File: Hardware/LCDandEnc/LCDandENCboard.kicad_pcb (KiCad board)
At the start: 2 copper layers, 18 parts, among them J1 LCD4x20, J2 LCD4x20, U1 74HC14

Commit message: layout and BOM
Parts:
- removed 1U2: 0,1U, Capacitors_SMD:C_0805_HandSoldering
- added C4: 1u, Capacitors_SMD:C_0805_HandSoldering, F.Cu at (160.9, 108.9)
- added C5: 100n, Capacitors_SMD:C_0805_HandSoldering, F.Cu at (161.0, 103.7)
- added REF**: JUMPER 5MM, Libs:JUMPER_5MM, F.Cu at (153.1, 112.4)
- added U2: XC6206P332MR, TO_SOT_Packages_SMD:TSOT-23_HandSoldering, F.Cu at (156.7, 106.2)
- J1: value LCD4x20 -> Connection to mainBoard; footprint Pin_Headers:Pin_Header_Straight_1x04_Pitch2.54mm -> Pin_Headers:Pin_Header_Straight_1x07_Pitch2.54mm
- moved 1U1 62.2 mm to (134.0, 107.1), turned to 90 degrees
- moved J1 61.2 mm to (133.0, 114.6), turned to 90 degrees
- moved J2 42.0 mm to (152.3, 114.6), turned to 90 degrees
- moved D1 24.0 mm to (155.8, 95.8)
- moved R2 22.0 mm to (152.5, 90.5), turned to 270 degrees
- moved C1 21.6 mm to (159.0, 95.5)
- moved ROT1 20.1 mm to (141.2, 77.7)
- moved R1 19.0 mm to (152.4, 95.8)
- moved U1 15.2 mm to (139.5, 105.0), turned to 180 degrees
- moved C3 13.9 mm to (150.0, 95.7), turned to 90 degrees
- moved R4 12.2 mm to (147.4, 87.5)
- moved R5 11.7 mm to (135.7, 94.8), turned to 270 degrees
- moved C2 9.68 mm to (130.0, 95.0), turned to 90 degrees
- moved D3 9.44 mm to (147.3, 95.6), turned to 90 degrees
- moved D2 7.96 mm to (132.9, 94.6), turned to 90 degrees
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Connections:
- 1U1 pad 1: VCC -> +3V3
- J1 pad 1: Rot_Enc_SW -> GND
- J1 pad 2: Rot_Enc_A -> Rot_Enc_B
- J1 pad 3: Rot_Enc_B -> Rot_Enc_A
- J1 pad 4: (no net) -> Rot_Enc_SW
- J2 pad 1: VCC -> +5V
- J2 pad 2: (no net) -> SCL
- J2 pad 3: (no net) -> SDA
- R2 pad 1: VCC -> +3V3
- R3 pad 1: VCC -> +3V3
- R4 pad 1: VCC -> +3V3
- U1 pad 14: VCC -> (no net)
- U1 pad 3: Net-(C2-Pad1) -> (no net)
- U1 pad 4: Rot_Enc_B -> (no net)
- U1 pad 8: (no net) -> Rot_Enc_B
- U1 pad 9: (no net) -> Net-(C2-Pad1)
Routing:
- net +3V3: track 0.00 -> 125.3 mm
- net GND: track 93.0 -> 123.9 mm
- net Net-(C2-Pad1): track 42.0 -> 14.0 mm
- net Net-(C1-Pad1): track 18.6 -> 39.5 mm
- net SCL: track 0.00 -> 18.8 mm
- net +5V: track 0.00 -> 16.5 mm
- net Rot_Enc_B: track 0.00 -> 16.1 mm
- net SDA: track 0.00 -> 15.0 mm
- net Rot_Enc_A: track 0.00 -> 14.6 mm
- net Net-(D1-Pad1): track 8.68 -> 20.4 mm
- net Net-(D2-Pad2): track 24.2 -> 14.9 mm
- net Rot_Enc_SW: track 0.00 -> 8.67 mm
- net VCC: track 8.47 -> 0.00 mm
- net Net-(D3-Pad2): track 20.5 -> 15.4 mm
- net Net-(C3-Pad1): track 14.0 -> 15.5 mm
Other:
- board outline added: 38 x 52.8 mm
- board text added: "LCD/ROTENC 25/3-18"

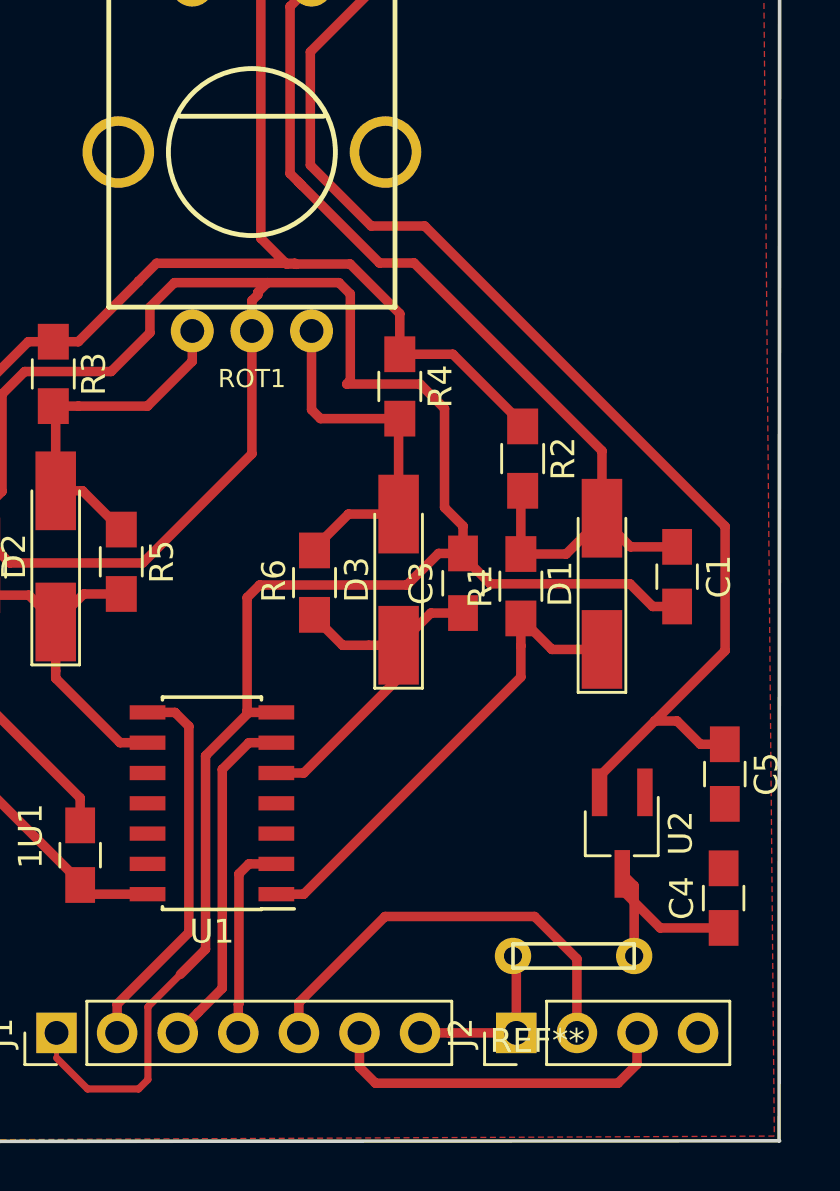
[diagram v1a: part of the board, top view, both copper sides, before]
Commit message: Bad I2C pinout
Swappe some pins around to match the i2c lcd board
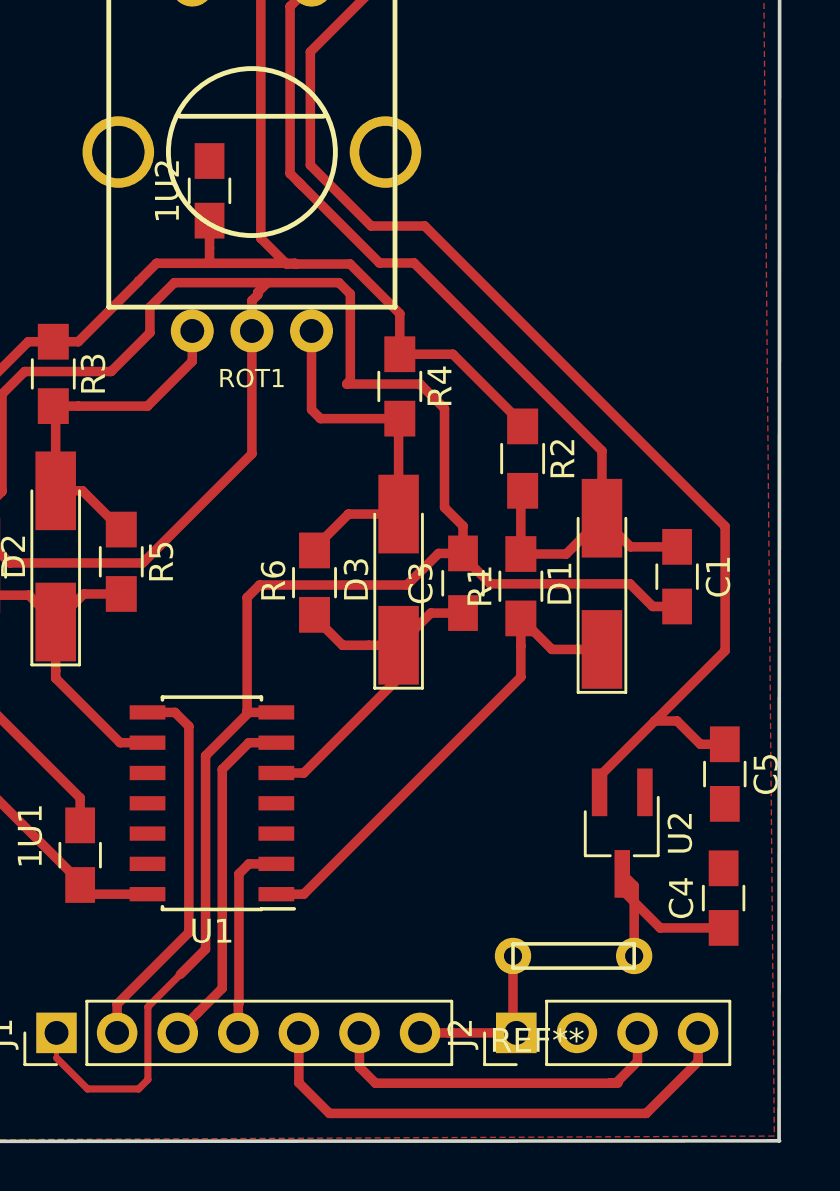
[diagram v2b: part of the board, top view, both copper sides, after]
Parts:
- added 1U2: 0,1U, Capacitors_SMD:C_0805_HandSoldering, F.Cu at (139.4, 79.3)
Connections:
- J2 pad 2: SCL -> GND
- J2 pad 4: GND -> SCL
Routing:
- net SCL: track 18.8 -> 21.5 mm
- net +3V3: track 125.3 -> 127.1 mm
- net GND: track 123.9 -> 124.4 mm
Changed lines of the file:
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@@
 (kicad_pcb (version 4) (host pcbnew 4.0.7)
   (general
-    (links 0)
-    (no_connects 8)
-    (area 125.25 66.299999 163.925 124.494048)
+    (links 46)
+    (no_connects 6)
+    (area 125.274999 66.299999 163.375001 119.200001)
     (thickness 1.6)
     (drawings 5)
-    (tracks 181)
+    (tracks 187)
     (zones 0)
-    (modules 21)
+    (modules 22)
     (nets 15)
   )
@@
       (net 13 +5V))
     (pad 2 thru_hole oval (at 0 2.54 90) (size 1.7 1.7) (drill 1) (layers *.Cu *.Mask)
-      (net 12 SCL))
+      (net 1 GND))
     (pad 3 thru_hole oval (at 0 5.08 90) (size 1.7 1.7) (drill 1) (layers *.Cu *.Mask)
       (net 14 SDA))
     (pad 4 thru_hole oval (at 0 7.62 90) (size 1.7 1.7) (drill 1) (layers *.Cu *.Mask)
-      (net 1 GND))
+      (net 12 SCL))
     (model ${KISYS3DMOD}/Pin_Headers.3dshapes/Pin_Header_Straight_1x04_Pitch2.54mm.wrl
       (at (xyz 0 0 0))
@@
     (pad 2 thru_hole circle (at 1.016 1.016 180) (size 1.524 1.524) (drill 0.762) (layers *.Cu *.Mask)
       (net 13 +5V))
+  )
+  (module Capacitors_SMD:C_0805_HandSoldering (layer F.Cu)
+    (at 139.4 79.275 90)
+    (descr "Capacitor SMD 0805, hand soldering")
+    (tags "capacitor 0805")
+    (attr smd)
+    (fp_text reference 1U2 (at 0 -1.75 90) (layer F.SilkS)
+      (effects (font (size 1 1) (thickness 0.15)))
+    )
+    (fp_text value 0,1U (at 0 1.75 90) (layer F.Fab)
+      (effects (font (size 1 1) (thickness 0.15)))
+    )
+    (fp_text user %R (at 0 -1.75 90) (layer F.Fab)
+      (effects (font (size 1 1) (thickness 0.15)))
+    )
+    (fp_line (start -1 0.62) (end -1 -0.62) (layer F.Fab) (width 0.1))
+    (fp_line (start 1 0.62) (end -1 0.62) (layer F.Fab) (width 0.1))
+    (fp_line (start 1 -0.62) (end 1 0.62) (layer F.Fab) (width 0.1))
+    (fp_line (start -1 -0.62) (end 1 -0.62) (layer F.Fab) (width 0.1))
+    (fp_line (start 0.5 -0.85) (end -0.5 -0.85) (layer F.SilkS) (width 0.12))
+    (fp_line (start -0.5 0.85) (end 0.5 0.85) (layer F.SilkS) (width 0.12))
+    (fp_line (start -2.25 -0.88) (end 2.25 -0.88) (layer F.CrtYd) (width 0.05))
+    (fp_line (start -2.25 -0.88) (end -2.25 0.87) (layer F.CrtYd) (width 0.05))
+    (fp_line (start 2.25 0.87) (end 2.25 -0.88) (layer F.CrtYd) (width 0.05))
+    (fp_line (start 2.25 0.87) (end -2.25 0.87) (layer F.CrtYd) (width 0.05))
+    (pad 1 smd rect (at -1.25 0 90) (size 1.5 1.25) (layers F.Cu F.Paste F.Mask)
+      (net 11 +3V3))
+    (pad 2 smd rect (at 1.25 0 90) (size 1.5 1.25) (layers F.Cu F.Paste F.Mask)
+      (net 1 GND))
+    (model Capacitors_SMD.3dshapes/C_0805.wrl
+      (at (xyz 0 0 0))
+      (scale (xyz 1 1 1))
+      (rotate (xyz 0 0 0))
+    )
   )
   (gr_text "LCD/ROTENC\n25/3-18" (at 156.75 76.25 90) (layer Cmts.User)
@@
   (segment (start 136.814999 113.485001) (end 136.814999 116.535001) (width 0.3) (layer F.Cu) (net 1))
   (segment (start 142.2 101.14) (end 141.05 101.14) (width 0.4) (layer F.Cu) (net 1))
+  (segment (start 154.424639 114.199639) (end 154.8 114.575) (width 0.4) (layer F.Cu) (net 1))
   (segment (start 142.775001 71.549999) (end 142.775001 78.550001) (width 0.4) (layer F.Cu) (net 2))
   (segment (start 142.775001 78.550001) (end 143.25 79.025) (width 0.4) (layer F.Cu) (net 2))
@@
   (segment (start 138.532335 101.722335) (end 138.532335 110.365584) (width 0.4) (layer F.Cu) (net 10))
   (segment (start 138.532335 110.365584) (end 135.525 113.372919) (width 0.4) (layer F.Cu) (net 10))
+  (segment (start 137.179005 82.311184) (end 139.4 82.311184) (width 0.4) (layer F.Cu) (net 11))
+  (segment (start 139.4 82.311184) (end 142.975351 82.311184) (width 0.4) (layer F.Cu) (net 11))
+  (segment (start 139.4 80.525) (end 139.4 81.675) (width 0.4) (layer F.Cu) (net 11))
+  (segment (start 139.4 81.675) (end 139.4 82.311184) (width 0.4) (layer F.Cu) (net 11))
   (segment (start 141.55 69.175) (end 141.55 81.267016) (width 0.4) (layer F.Cu) (net 11))
   (segment (start 145.025 68.55) (end 142.175 68.55) (width 0.4) (layer F.Cu) (net 11))
@@
   (segment (start 136.428014 83.062175) (end 137.179005 82.311184) (width 0.4) (layer F.Cu) (net 11))
   (segment (start 142.975351 82.311184) (end 143.022249 82.358082) (width 0.4) (layer F.Cu) (net 11))
-  (segment (start 137.179005 82.311184) (end 142.975351 82.311184) (width 0.4) (layer F.Cu) (net 11))
   (segment (start 155.75 104.49) (end 155.75 103.815) (width 0.4) (layer F.Cu) (net 11))
   (segment (start 161.012593 98.552407) (end 161.012593 93.342495) (width 0.4) (layer F.Cu) (net 11))
@@
   (segment (start 149.6 86.125) (end 147.375 86.125) (width 0.4) (layer F.Cu) (net 11))
   (segment (start 152.525 89.15) (end 152.525 89.05) (width 0.4) (layer F.Cu) (net 11))
-  (segment (start 154.8 114.575) (end 154.8 111.468309) (width 0.4) (layer F.Cu) (net 12))
-  (segment (start 143.145 113.307146) (end 143.145 114.575) (width 0.4) (layer F.Cu) (net 12))
-  (segment (start 154.8 111.468309) (end 153.026447 109.694756) (width 0.4) (layer F.Cu) (net 12))
-  (segment (start 153.026447 109.694756) (end 146.75739 109.694756) (width 0.4) (layer F.Cu) (net 12))
-  (segment (start 146.75739 109.694756) (end 143.145 113.307146) (width 0.4) (layer F.Cu) (net 12))
-  (segment (start 154.424639 114.199639) (end 154.8 114.575) (width 0.4) (layer F.Cu) (net 12))
+  (segment (start 144.425 117.95) (end 143.145 116.67) (width 0.4) (layer F.Cu) (net 12))
+  (segment (start 143.145 116.67) (end 143.145 114.575) (width 0.4) (layer F.Cu) (net 12))
+  (segment (start 157.707081 117.95) (end 144.425 117.95) (width 0.4) (layer F.Cu) (net 12))
+  (segment (start 159.88 114.575) (end 159.88 115.777081) (width 0.4) (layer F.Cu) (net 12))
+  (segment (start 159.88 115.777081) (end 157.707081 117.95) (width 0.4) (layer F.Cu) (net 12))
+  (segment (start 152.12 111.35) (end 152.12 114.435) (width 0.4) (layer F.Cu) (net 13))
+  (segment (start 152.12 114.435) (end 152.26 114.575) (width 0.4) (layer F.Cu) (net 13))
+  (segment (start 149.427081 114.575) (end 152.26 114.575) (width 0.4) (layer F.Cu) (net 13))
   (segment (start 160.95 110.175) (end 158.29 110.175) (width 0.4) (layer F.Cu) (net 13))
   (segment (start 158.29 110.175) (end 156.7 108.585) (width 0.4) (layer F.Cu) (net 13))
@@
   (segment (start 157.2 111.35) (end 157.2 108.41) (width 0.4) (layer F.Cu) (net 13))
   (segment (start 157.2 108.41) (end 156.7 107.91) (width 0.4) (layer F.Cu) (net 13))
-  (segment (start 152.26 114.575) (end 152.26 111.49) (width 0.4) (layer F.Cu) (net 13))
   (segment (start 152.26 111.49) (end 152.12 111.35) (width 0.4) (layer F.Cu) (net 13))
   (segment (start 148.225 114.575) (end 149.427081 114.575) (width 0.4) (layer F.Cu) (net 13))
-  (segment (start 149.427081 114.575) (end 152.26 114.575) (width 0.4) (layer F.Cu) (net 13))
+  (segment (start 146.357736 116.683856) (end 156.175 116.683856) (width 0.4) (layer F.Cu) (net 14))
+  (segment (start 157.34 114.575) (end 157.34 115.777081) (width 0.4) (layer F.Cu) (net 14))
+  (segment (start 156.175 116.683856) (end 156.522625 116.683856) (width 0.4) (layer F.Cu) (net 14))
+  (segment (start 157.34 115.777081) (end 156.433225 116.683856) (width 0.4) (layer F.Cu) (net 14))
+  (segment (start 156.433225 116.683856) (end 156.175 116.683856) (width 0.4) (layer F.Cu) (net 14))
   (segment (start 145.685 114.575) (end 145.685 116.01112) (width 0.4) (layer F.Cu) (net 14))
   (segment (start 145.685 116.01112) (end 146.357736 116.683856) (width 0.4) (layer F.Cu) (net 14))
-  (segment (start 146.357736 116.683856) (end 156.522625 116.683856) (width 0.4) (layer F.Cu) (net 14))
-  (segment (start 156.522625 116.683856) (end 157.32045 115.886031) (width 0.4) (layer F.Cu) (net 14))
-  (segment (start 157.32045 115.886031) (end 157.32045 114.59455) (width 0.4) (layer F.Cu) (net 14))
   (segment (start 157.32045 114.59455) (end 157.34 114.575) (width 0.4) (layer F.Cu) (net 14))
   (zone (net 1) (net_name GND) (layer F.Cu) (hatch edge 0.508)

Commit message: PCB
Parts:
- added REF**: MountingHole_3.2mm_M3_DIN965_Pad, Mounting_Holes:MountingHole_3.2mm_M3_DIN965_Pad, F.Cu at (158.7, 71.5)
- added REF**: MountingHole_3.2mm_M3_DIN965_Pad, Mounting_Holes:MountingHole_3.2mm_M3_DIN965_Pad, F.Cu at (130.2, 71.4)
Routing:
- net GND: track 124.4 -> 196.9 mm
- net SCL: track 21.5 -> 19.4 mm
- net +3V3: track 127.1 -> 128.3 mm
- net Net-(C1-Pad1): track 39.5 -> 40.1 mm
